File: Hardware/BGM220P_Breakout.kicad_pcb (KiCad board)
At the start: 4 copper layers, 31 x 31 mm, 4 parts, among them J1 Conn_01x16, J2 Conn_01x16, J3 Conn_02x05_Odd_Even, U1 BGM220P

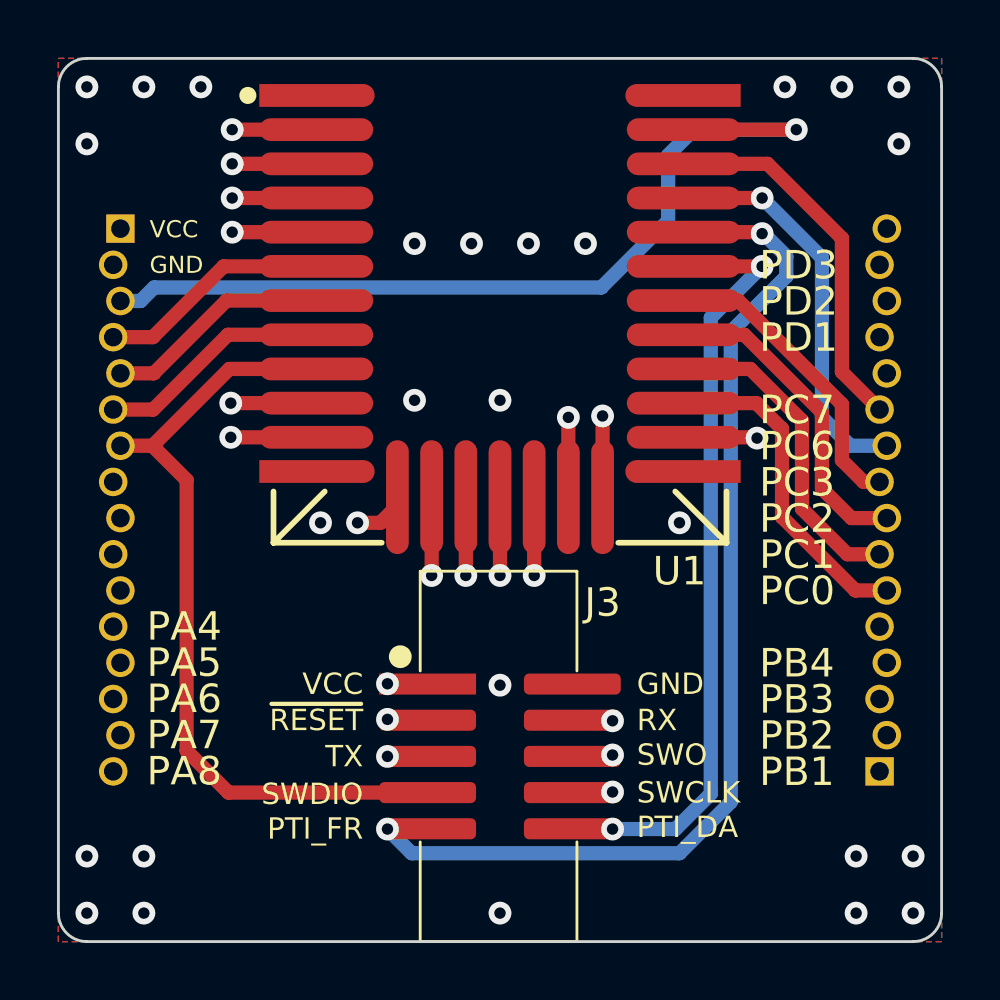
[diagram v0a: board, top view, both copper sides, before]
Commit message: Increasing via diameter to 0.5mm
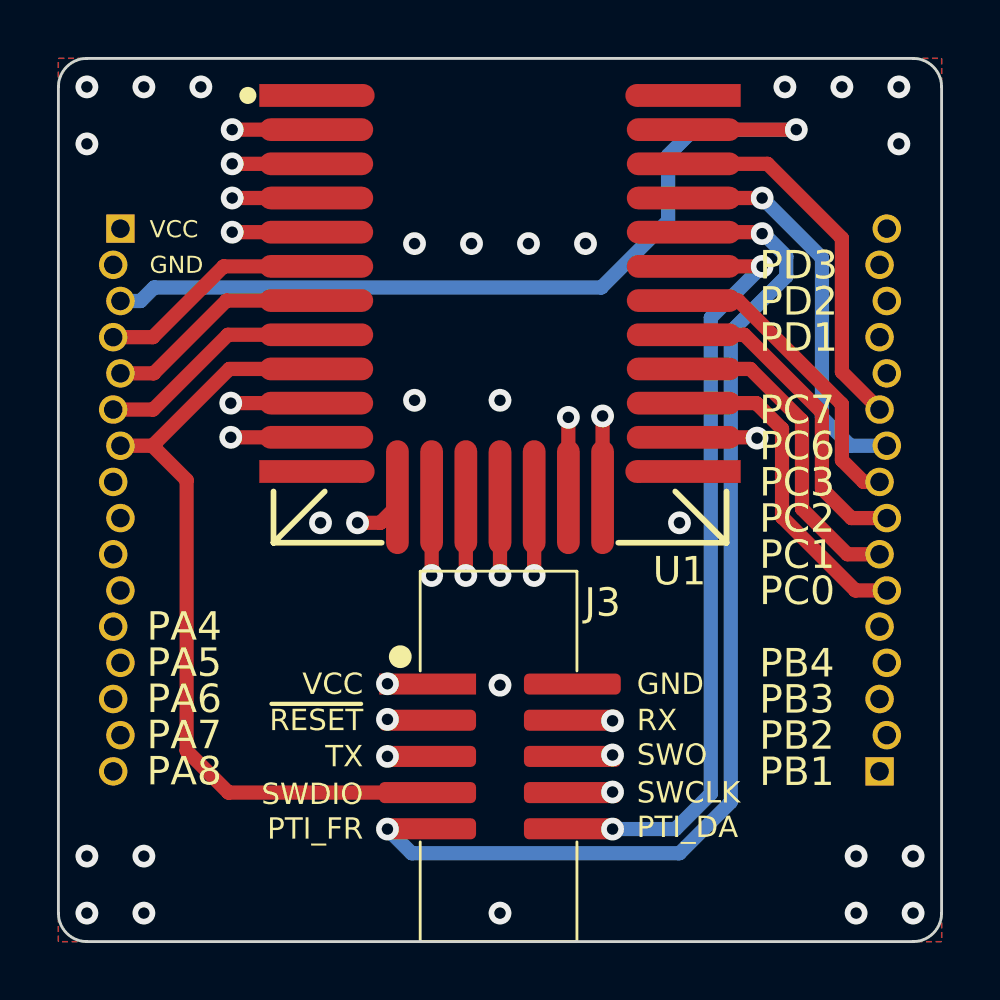
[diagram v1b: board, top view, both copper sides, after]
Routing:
- net VCC: track 3.95 -> 1.65 mm
- net SWO: track 34.8 -> 32.8 mm
- net SWCLK: track 48.2 -> 46.2 mm
- net VCOM_RX: track 39.4 -> 37.4 mm
- net PTI_FRAME: track 56.4 -> 54.4 mm
- net PTI_DATA: track 53.3 -> 51.3 mm
- net VCOM_TX: track 30.9 -> 28.9 mm
- net ~{RESET}: track 63.8 -> 61.8 mm
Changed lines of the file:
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@@
   )
   (segment (start 95.8 100.8) (end 96.4 100.2) (width 0.5) (layer "F.Cu") (net 1))
-  (segment (start 96.06 106.46) (end 96.05 106.45) (width 0.5) (layer "F.Cu") (net 1))
-  (segment (start 96.4 100.2) (end 96.4 99.9) (width 0.5) (layer "F.Cu") (net 1))
-  (segment (start 98.05 106.46) (end 96.06 106.46) (width 0.5) (layer "F.Cu") (net 1))
   (segment (start 95 100.8) (end 95.8 100.8) (width 0.5) (layer "F.Cu") (net 1))
   (via (at 95 100.8) (size 0.8) (drill 0.4) (layers "F.Cu" "B.Cu") (net 1))
@@
   (via (at 99 91) (size 0.8) (drill 0.4) (layers "F.Cu" "B.Cu") (free) (net 2))
   (segment (start 110.4 87) (end 106.45 87) (width 0.5) (layer "F.Cu") (net 3))
-  (segment (start 98.02 107.7) (end 96.05 107.7) (width 0.5) (layer "F.Cu") (net 3))
   (via (at 96.05 107.7) (size 0.8) (drill 0.4) (layers "F.Cu" "B.Cu") (net 3))
   (via (at 110.4 87) (size 0.8) (drill 0.4) (layers "F.Cu" "B.Cu") (net 3))
@@
   (segment (start 105.9 87.9) (end 106.8 87) (width 0.5) (layer "B.Cu") (net 3))
   (segment (start 106.8 87) (end 110.4 87) (width 0.5) (layer "B.Cu") (net 3))
-  (segment (start 103.93 107.73) (end 103.95 107.75) (width 0.5) (layer "F.Cu") (net 4))
-  (segment (start 101.95 107.73) (end 103.93 107.73) (width 0.5) (layer "F.Cu") (net 4))
   (segment (start 87.815 94.285) (end 86.423 94.285) (width 0.5) (layer "F.Cu") (net 4))
   (segment (start 90.3 91.8) (end 87.815 94.285) (width 0.5) (layer "F.Cu") (net 4))
@@
   (segment (start 86.677 95.555) (end 87.845 95.555) (width 0.5) (layer "F.Cu") (net 5))
   (segment (start 87.845 95.555) (end 90.4 93) (width 0.5) (layer "F.Cu") (net 5))
-  (segment (start 98.05 109) (end 96.05 109) (width 0.5) (layer "F.Cu") (net 5))
   (via (at 96.05 109) (size 0.8) (drill 0.4) (layers "F.Cu" "B.Cu") (net 5))
   (segment (start 94.7 109) (end 96.05 109) (width 0.5) (layer "In1.Cu") (net 5))
@@
   (segment (start 92 106.3) (end 94.7 109) (width 0.5) (layer "In1.Cu") (net 5))
   (segment (start 92 96) (end 91.555 95.555) (width 0.5) (layer "In1.Cu") (net 5))
-  (segment (start 101.95 109) (end 103.9 109) (width 0.5) (layer "F.Cu") (net 6))
   (segment (start 93.55 96.6) (end 90.55 96.6) (width 0.5) (layer "F.Cu") (net 6))
-  (segment (start 103.9 109) (end 103.95 108.95) (width 0.5) (layer "F.Cu") (net 6))
   (via (at 103.95 108.95) (size 0.8) (drill 0.4) (layers "F.Cu" "B.Cu") (net 6))
   (via (at 90.55 96.6) (size 0.8) (drill 0.4) (layers "F.Cu" "B.Cu") (net 6))
@@
   (segment (start 88.7 98.4) (end 88.7 97.3) (width 0.5) (layer "In1.Cu") (net 6))
   (segment (start 89 99.3) (end 89 108.8) (width 0.5) (layer "F.Cu") (net 7))
-  (segment (start 93.55 95.4) (end 90.8 95.4) (width 0.5) (layer "F.Cu") (net 7))
+  (segment (start 90.5 95.4) (end 93.55 95.4) (width 0.5) (layer "F.Cu") (net 7))
   (segment (start 87.795 98.095) (end 89 99.3) (width 0.5) (layer "F.Cu") (net 7))
   (segment (start 87.795 98.095) (end 87.805 98.095) (width 0.5) (layer "F.Cu") (net 7))
@@
   (segment (start 90.47 110.27) (end 98.05 110.27) (width 0.5) (layer "F.Cu") (net 7))
   (segment (start 86.677 98.095) (end 87.795 98.095) (width 0.5) (layer "F.Cu") (net 7))
-  (segment (start 90.5 95.4) (end 90.8 95.4) (width 0.5) (layer "F.Cu") (net 7))
   (segment (start 89 108.8) (end 90.47 110.27) (width 0.5) (layer "F.Cu") (net 7))
   (segment (start 86.423 96.825) (end 87.825 96.825) (width 0.5) (layer "F.Cu") (net 8))
   (segment (start 90.45 94.2) (end 93.55 94.2) (width 0.5) (layer "F.Cu") (net 8))
-  (segment (start 101.95 110.27) (end 103.93 110.27) (width 0.5) (layer "F.Cu") (net 8))
-  (segment (start 103.93 110.27) (end 103.95 110.25) (width 0.5) (layer "F.Cu") (net 8))
   (segment (start 87.825 96.825) (end 90.45 94.2) (width 0.5) (layer "F.Cu") (net 8))
   (via (at 103.95 110.25) (size 0.8) (drill 0.4) (layers "F.Cu" "B.Cu") (net 8))
@@
   (segment (start 104.7 112.4) (end 104.9 112.2) (width 0.5) (layer "In1.Cu") (net 8))
   (segment (start 85.2 97.3) (end 85.2 109.7) (width 0.5) (layer "In1.Cu") (net 8))
-  (segment (start 96.05 111.55) (end 96.06 111.54) (width 0.5) (layer "F.Cu") (net 9))
   (segment (start 109.15 90.6) (end 109.2 90.65) (width 0.5) (layer "F.Cu") (net 9))
   (segment (start 106.45 90.6) (end 109.15 90.6) (width 0.5) (layer "F.Cu") (net 9))
-  (segment (start 96.06 111.54) (end 98.05 111.54) (width 0.5) (layer "F.Cu") (net 9))
   (via (at 96.05 111.55) (size 0.8) (drill 0.4) (layers "F.Cu" "B.Cu") (net 9))
   (via (at 109.2 90.65) (size 0.8) (drill 0.4) (layers "F.Cu" "B.Cu") (net 9))
@@
   (segment (start 96.9 112.4) (end 106.3 112.4) (width 0.5) (layer "B.Cu") (net 9))
   (segment (start 106.45 91.8) (end 109.2 91.8) (width 0.5) (layer "F.Cu") (net 10))
-  (segment (start 101.95 111.54) (end 103.94 111.54) (width 0.5) (layer "F.Cu") (net 10))
-  (segment (start 103.94 111.54) (end 103.95 111.55) (width 0.5) (layer "F.Cu") (net 10))
   (via (at 103.95 111.55) (size 0.8) (drill 0.4) (layers "F.Cu" "B.Cu") (net 10))
   (via (at 109.2 91.8) (size 0.8) (drill 0.4) (layers "F.Cu" "B.Cu") (net 10))
@@
   (segment (start 102.4 99.9) (end 102.4 97.1) (width 0.5) (layer "F.Cu") (net 17))
   (via (at 102.4 97.1) (size 0.8) (drill 0.4) (layers "F.Cu" "B.Cu") (net 17))
-  (segment (start 110.655 91.745) (end 108.95 93.45) (width 0.5) (layer "In2.Cu") (net 17))
+  (segment (start 107.35 95.05) (end 110.655 91.745) (width 0.5) (layer "In2.Cu") (net 17))
   (segment (start 107.35 95.05) (end 103.2 95.05) (width 0.5) (layer "In2.Cu") (net 17))
   (segment (start 102.4 95.85) (end 102.4 97.1) (width 0.5) (layer "In2.Cu") (net 17))
   (segment (start 113.323 91.745) (end 110.655 91.745) (width 0.5) (layer "In2.Cu") (net 17))
   (segment (start 103.2 95.05) (end 102.4 95.85) (width 0.5) (layer "In2.Cu") (net 17))
-  (segment (start 108.95 93.45) (end 107.35 95.05) (width 0.5) (layer "In2.Cu") (net 17))
   (segment (start 103.6 99.9) (end 103.6 97.05) (width 0.5) (layer "F.Cu") (net 18))
   (via (at 103.6 97.05) (size 0.8) (drill 0.4) (layers "F.Cu" "B.Cu") (net 18))
@@
   (segment (start 103.95 95.75) (end 107.63995 95.75) (width 0.5) (layer "In2.Cu") (net 18))
   (segment (start 113.577 93.015) (end 110.37495 93.015) (width 0.5) (layer "In2.Cu") (net 18))
-  (segment (start 107.63995 95.75) (end 109.294975 94.094975) (width 0.5) (layer "In2.Cu") (net 18))
+  (segment (start 107.63995 95.75) (end 110.37495 93.015) (width 0.5) (layer "In2.Cu") (net 18))
   (segment (start 103.6 97.05) (end 103.6 96.1) (width 0.5) (layer "In2.Cu") (net 18))
-  (segment (start 110.37495 93.015) (end 109.294975 94.094975) (width 0.5) (layer "In2.Cu") (net 18))
   (segment (start 106.45 97.8) (end 108.99385 97.8) (width 0.5) (layer "F.Cu") (net 19))
   (segment (start 108.99385 97.8) (end 109.021925 97.828075) (width 0.5) (layer "F.Cu") (net 19))
